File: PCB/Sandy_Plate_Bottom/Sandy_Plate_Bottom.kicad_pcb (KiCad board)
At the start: 2 copper layers, 285 x 94.6 mm, 9 parts

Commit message: 調整：3Dチェック用STEPファイル出力時の基板原点合わせ
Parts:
- added REF**: 1U, locallib:MXOnly-1U-Hotswap-guide-dummy, F.Cu at (24.6, 26.3)
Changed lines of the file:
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@@
   (setup
     (pad_to_mask_clearance 0)
+    (grid_origin 15.075 16.77504)
     (pcbplotparams
       (layerselection 0x00010fc_ffffffff)
@@
       (stroke (width 0.01) (type solid)) (fill solid) (layer "F.SilkS"))
   )
+  (footprint "locallib:MXOnly-1U-Hotswap-guide-dummy" locked (layer "F.Cu")
+    (at 24.6 26.30004)
+    (attr smd board_only)
+    (fp_text reference "REF**" (at 0 3.048) (layer "B.CrtYd")
+        (effects (font (size 1 1) (thickness 0.15)) (justify mirror))
+    )
+    (fp_text value "1U" (at 0 -7.9375) (layer "Dwgs.User")
+        (effects (font (size 1 1) (thickness 0.15)))
+    )
+    (fp_line (start -9.525 -9.525) (end 9.525 -9.525)
+      (stroke (width 0.15) (type solid)) (layer "Dwgs.User"))
+    (fp_line (start -9.525 9.525) (end -9.525 -9.525)
+      (stroke (width 0.15) (type solid)) (layer "Dwgs.User"))
+    (fp_line (start -8.382 -3.81) (end -8.382 -1.27)
+      (stroke (width 0.15) (type solid)) (layer "Dwgs.User"))
+    (fp_line (start -8.382 -1.27) (end -5.842 -1.27)
+      (stroke (width 0.15) (type solid)) (layer "Dwgs.User"))
+    (fp_line (start -7 -7) (end -7 -5)
+      (stroke (width 0.15) (type solid)) (layer "Dwgs.User"))
+    (fp_line (start -7 5) (end -7 7)
+      (stroke (width 0.15) (type solid)) (layer "Dwgs.User"))
+    (fp_line (start -7 7) (end -5 7)
+      (stroke (width 0.15) (type solid)) (layer "Dwgs.User"))
+    (fp_line (start -6.1 -4.85) (end -6.1 -0.905)
+      (stroke (width 0.15) (type solid)) (layer "Dwgs.User"))
+    (fp_line (start -6.1 -0.896) (end -2.49 -0.896)
+      (stroke (width 0.15) (type solid)) (layer "Dwgs.User"))
+    (fp_line (start -5.842 -3.81) (end -8.382 -3.81)
+      (stroke (width 0.15) (type solid)) (layer "Dwgs.User"))
+    (fp_line (start -5.842 -1.27) (end -5.842 -3.81)
+      (stroke (width 0.15) (type solid)) (layer "Dwgs.User"))
+    (fp_line (start -5 -7) (end -7 -7)
+      (stroke (width 0.15) (type solid)) (layer "Dwgs.User"))
+    (fp_line (start 4.572 -6.35) (end 7.112 -6.35)
+      (stroke (width 0.15) (type solid)) (layer "Dwgs.User"))
+    (fp_line (start 4.572 -3.81) (end 4.572 -6.35)
+      (stroke (width 0.15) (type solid)) (layer "Dwgs.User"))
+    (fp_line (start 4.8 -6.804) (end -3.825 -6.804)
+      (stroke (width 0.15) (type solid)) (layer "Dwgs.User"))
+    (fp_line (start 4.8 -2.896) (end 4.8 -6.804)
+      (stroke (width 0.15) (type solid)) (layer "Dwgs.User"))
+    (fp_line (start 4.8 -2.85) (end -0.25 -2.804)
+      (stroke (width 0.15) (type solid)) (layer "Dwgs.User"))
+    (fp_line (start 5 -7) (end 7 -7)
+      (stroke (width 0.15) (type solid)) (layer "Dwgs.User"))
+    (fp_line (start 5 7) (end 7 7)
+      (stroke (width 0.15) (type solid)) (layer "Dwgs.User"))
+    (fp_line (start 7 -7) (end 7 -5)
+      (stroke (width 0.15) (type solid)) (layer "Dwgs.User"))
+    (fp_line (start 7 7) (end 7 5)
+      (stroke (width 0.15) (type solid)) (layer "Dwgs.User"))
+    (fp_line (start 7.112 -6.35) (end 7.112 -3.81)
+      (stroke (width 0.15) (type solid)) (layer "Dwgs.User"))
+    (fp_line (start 7.112 -3.81) (end 4.572 -3.81)
+      (stroke (width 0.15) (type solid)) (layer "Dwgs.User"))
+    (fp_line (start 9.525 -9.525) (end 9.525 9.525)
+      (stroke (width 0.15) (type solid)) (layer "Dwgs.User"))
+    (fp_line (start 9.525 9.525) (end -9.525 9.525)
+      (stroke (width 0.15) (type solid)) (layer "Dwgs.User"))
+    (fp_arc (start -6.089 -4.92) (mid -5.347189 -6.33089) (end -3.825 -6.804)
+      (stroke (width 0.15) (type solid)) (layer "Dwgs.User"))
+    (fp_arc (start -2.485 -0.92) (mid -1.744361 -2.328061) (end -0.225 -2.8)
+      (stroke (width 0.15) (type solid)) (layer "Dwgs.User"))
+    (fp_circle (center -5.1 0) (end -4.5 0.6)
+      (stroke (width 0.12) (type solid)) (fill none) (layer "Dwgs.User"))
+    (fp_circle (center -3.81 -2.54) (end -2.286 -2.54)
+      (stroke (width 0.15) (type solid)) (fill none) (layer "Dwgs.User"))
+    (fp_circle (center 0 0) (end 2 0)
+      (stroke (width 0.12) (type solid)) (fill none) (layer "Dwgs.User"))
+    (fp_circle (center 2.54 -5.08) (end 4.064 -5.08)
+      (stroke (width 0.15) (type solid)) (fill none) (layer "Dwgs.User"))
+    (fp_circle (center 5.1 0) (end 5.7 0.6)
+      (stroke (width 0.12) (type solid)) (fill none) (layer "Dwgs.User"))
+  )
   (footprint "locallib:Sandy_logo_w24" (layer "F.Cu")
     (at 245.26875 66.675)
@@
   (gr_line (start 10.375 27.35) (end 307.025 27.35)
     (stroke (width 0.15) (type dash)) (layer "B.SilkS"))
-  (gr_circle (center 25.7 35.2) (end 35.2 35.2)
-    (stroke (width 0.12) (type solid)) (fill none) (layer "B.SilkS"))
   (gr_line (start 25.7 115.2) (end 25.7 14.4)
     (stroke (width 0.15) (type dash)) (layer "B.SilkS"))

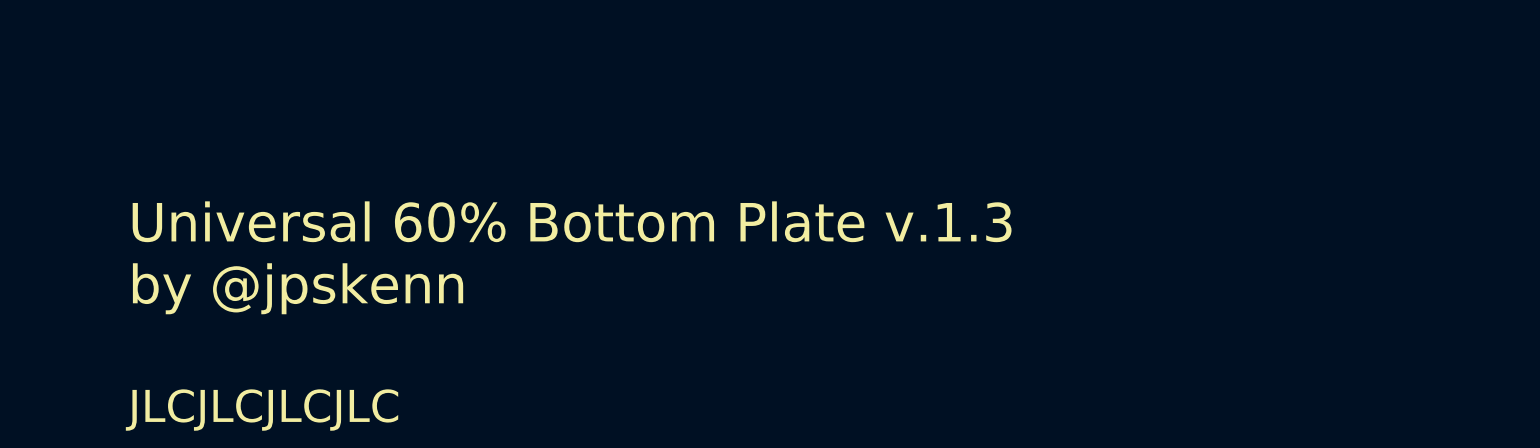
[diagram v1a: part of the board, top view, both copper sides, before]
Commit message: 変更：あまり使わなそうなガイドラインを削除
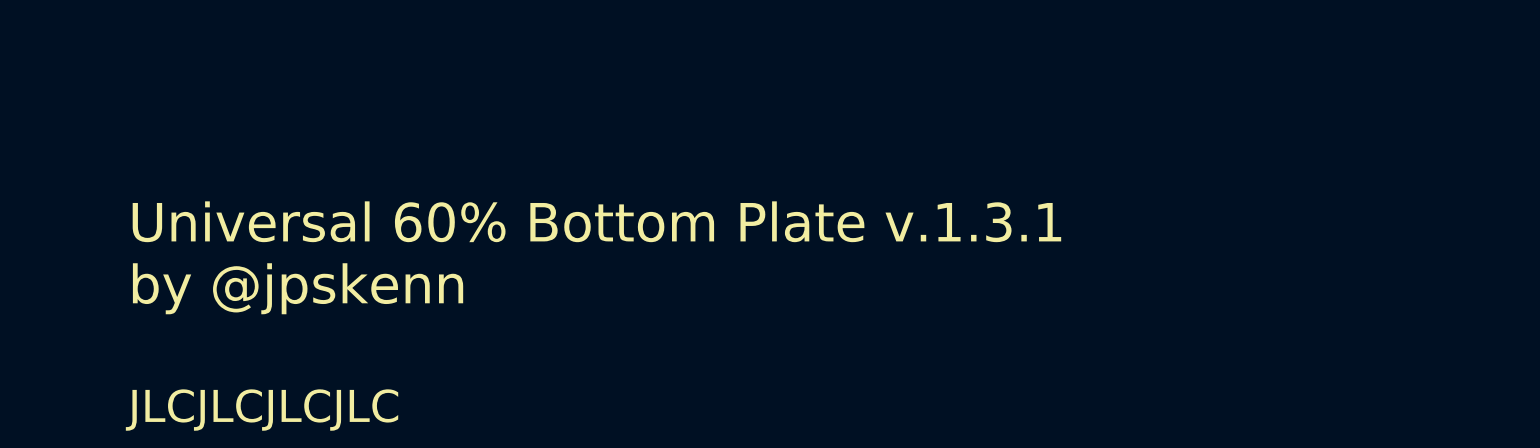
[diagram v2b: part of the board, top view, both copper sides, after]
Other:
- board text added: "Universal 60% Bottom Plate v.1.3.1 by @jpskenn"
- board text removed: "Universal 60% Bottom Plate v.1.3 by @jpskenn"
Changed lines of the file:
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@@
       (stroke (width 0) (type solid)) (fill solid) (layer "F.SilkS"))
   )
-  (gr_line (start 157.925 146.5) (end 157.925 4)
+  (gr_line (start 157.925 114.40629) (end 157.925 4)
     (stroke (width 0.15) (type dash)) (layer "B.SilkS"))
   (gr_line (start 15.575 21.875) (end 307.575 21.875)
-    (stroke (width 0.15) (type solid)) (layer "B.SilkS"))
+    (stroke (width 0.15) (type dot)) (layer "B.SilkS"))
   (gr_line (start 295.65 114.3) (end 295.65 13.5)
     (stroke (width 0.15) (type solid)) (layer "B.SilkS"))
@@
   (gr_circle (center 25.786697 27.341705) (end 35.286697 27.341705)
     (stroke (width 0.12) (type dash)) (fill none) (layer "B.SilkS"))
-  (gr_line (start 103.792505 146.071875) (end 103.792505 3.571875)
+  (gr_line (start 50.025 154.88754) (end 50.025 12.38754)
     (stroke (width 0.2) (type dot)) (layer "B.SilkS"))
   (gr_circle (center 20.2 21.875) (end 24.2 21.875)
@@
   (gr_circle (center 157.919253 48.8) (end 161.919253 48.8)
     (stroke (width 0.2) (type dot)) (fill none) (layer "B.SilkS"))
-  (gr_circle (center 212.094253 21.86) (end 216.094253 21.86)
-    (stroke (width 0.12) (type dash)) (fill none) (layer "B.SilkS"))
-  (gr_circle (center 103.792505 21.9) (end 107.792505 21.9)
-    (stroke (width 0.12) (type dash)) (fill none) (layer "B.SilkS"))
-  (gr_line (start 212.094253 146.071875) (end 212.094253 3.571875)
+  (gr_line (start 265.8 154.51254) (end 265.8 12.01254)
     (stroke (width 0.2) (type dot)) (layer "B.SilkS"))
   (gr_circle (center 157.925 106.9) (end 161.925 106.9)
     (stroke (width 0.12) (type solid)) (fill none) (layer "B.SilkS"))
-  (gr_line (start 9.594253 48.8) (end 306.244253 48.8)
-    (stroke (width 0.2) (type dot)) (layer "B.SilkS"))
   (gr_circle (center 295.65 106.9) (end 299.65 106.9)
     (stroke (width 0.12) (type solid)) (fill none) (layer "B.SilkS"))
@@
   (gr_circle (center 40.62 44.97) (end 42.65 46.1)
     (stroke (width 0.15) (type solid)) (fill none) (layer "Eco1.User"))
-  (gr_text "Universal 60% Bottom Plate v.1.3\nby @jpskenn" (at 70.246875 66.675) (layer "F.SilkS")
+  (gr_text "Universal 60% Bottom Plate v.1.3.1\nby @jpskenn" (at 70.246875 66.675) (layer "F.SilkS")
     (effects (font (size 1.8 1.8) (thickness 0.24)) (justify left))
   )
